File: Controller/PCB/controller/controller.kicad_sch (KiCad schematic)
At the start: 57 parts, among them J1 nRF24L01_Conn, Q1 S9013, Q2 S9013, Q4 S9013, SW1 SW_SPDT, U1 Joystick, U2 Joystick, U3 LM2940-3.0, U5 LM2940-5.0

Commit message: Finalise PCB Design
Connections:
- net Earth: now also U1.EARTH, U2.EARTH
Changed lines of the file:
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@@
     (pin "2")
-  )
-  (symbol (lib_id "power:Earth") (at 68.58 123.19 0) (unit 1)
-    (in_bom yes) (on_board yes)
-    (property "Reference" "#PWR0154" (id 0) (at 68.58 129.54 0)
-      (effects (font (size 1.27 1.27)) hide)
-    )
-    (property "Value" "Earth" (id 1) (at 68.58 127 0)
-      (effects (font (size 1.27 1.27)) hide)
-    )
-    (property "Footprint" "" (id 2) (at 68.58 123.19 0)
-      (effects (font (size 1.27 1.27)) hide)
-    )
-    (property "Datasheet" "~" (id 3) (at 68.58 123.19 0)
-      (effects (font (size 1.27 1.27)) hide)
-    )
-    (pin "1")
   )
   (symbol (lib_id "Device:LED") (at 232.41 22.86 90) (unit 1)
@@
     (pin "1")
     (pin "2")
+  )
+  (symbol (lib_id "power:Earth") (at 68.58 123.19 0) (unit 1)
+    (in_bom yes) (on_board yes)
+    (property "Reference" "#PWR0119" (id 0) (at 68.58 129.54 0)
+      (effects (font (size 1.27 1.27)) hide)
+    )
+    (property "Value" "Earth" (id 1) (at 68.58 127 0)
+      (effects (font (size 1.27 1.27)) hide)
+    )
+    (property "Footprint" "" (id 2) (at 68.58 123.19 0)
+      (effects (font (size 1.27 1.27)) hide)
+    )
+    (property "Datasheet" "~" (id 3) (at 68.58 123.19 0)
+      (effects (font (size 1.27 1.27)) hide)
+    )
+    (pin "1")
   )
   (symbol (lib_id "Device:R") (at 184.15 25.4 180) (unit 1)
@@
     (pin "1")
   )
+  (symbol (lib_id "power:Earth") (at 68.58 165.1 0) (unit 1)
+    (in_bom yes) (on_board yes)
+    (property "Reference" "#PWR0121" (id 0) (at 68.58 171.45 0)
+      (effects (font (size 1.27 1.27)) hide)
+    )
+    (property "Value" "Earth" (id 1) (at 68.58 168.91 0)
+      (effects (font (size 1.27 1.27)) hide)
+    )
+    (property "Footprint" "" (id 2) (at 68.58 165.1 0)
+      (effects (font (size 1.27 1.27)) hide)
+    )
+    (property "Datasheet" "~" (id 3) (at 68.58 165.1 0)
+      (effects (font (size 1.27 1.27)) hide)
+    )
+    (pin "1")
+  )
   (symbol (lib_id "Regulator_Linear:LM1117-5.0") (at 251.46 91.44 0) (unit 1)
     (in_bom yes) (on_board yes)
@@
     (pin "2")
   )
-  (symbol (lib_id "power:Earth") (at 68.58 165.1 0) (unit 1)
-    (in_bom yes) (on_board yes)
-    (property "Reference" "#PWR0155" (id 0) (at 68.58 171.45 0)
-      (effects (font (size 1.27 1.27)) hide)
-    )
-    (property "Value" "Earth" (id 1) (at 68.58 168.91 0)
-      (effects (font (size 1.27 1.27)) hide)
-    )
-    (property "Footprint" "" (id 2) (at 68.58 165.1 0)
-      (effects (font (size 1.27 1.27)) hide)
-    )
-    (property "Datasheet" "~" (id 3) (at 68.58 165.1 0)
-      (effects (font (size 1.27 1.27)) hide)
-    )
-    (pin "1")
-  )
   (symbol (lib_id "power:Earth") (at 151.13 123.19 0) (unit 1)
     (in_bom yes) (on_board yes)
@@
       (reference "#PWR0118") (unit 1) (value "+3.3V") (footprint "")
     )
+    (path "/6454f7b0-7b11-437e-b10a-8dd84dd76148"
+      (reference "#PWR0119") (unit 1) (value "Earth") (footprint "")
+    )
     (path "/00000000-0000-0000-0000-00006213857b"
       (reference "#PWR0120") (unit 1) (value "+3.3V") (footprint "")
     )
+    (path "/76caffeb-621d-4bb0-aa34-92fdde0764be"
+      (reference "#PWR0121") (unit 1) (value "Earth") (footprint "")
+    )
     (path "/00000000-0000-0000-0000-00006208d21d"
       (reference "#PWR0123") (unit 1) (value "+5V") (footprint "")
@@
       (reference "#PWR0153") (unit 1) (value "+BATT") (footprint "")
     )
-    (path "/2c8b76b6-1dc1-42a3-a2cc-221d9612c107"
-      (reference "#PWR0154") (unit 1) (value "Earth") (footprint "")
-    )
-    (path "/cc071879-20c2-476a-8fa9-027c97c88a6e"
-      (reference "#PWR0155") (unit 1) (value "Earth") (footprint "")
-    )
     (path "/8d4725e8-66fd-4c8d-af14-f62e909630d9"

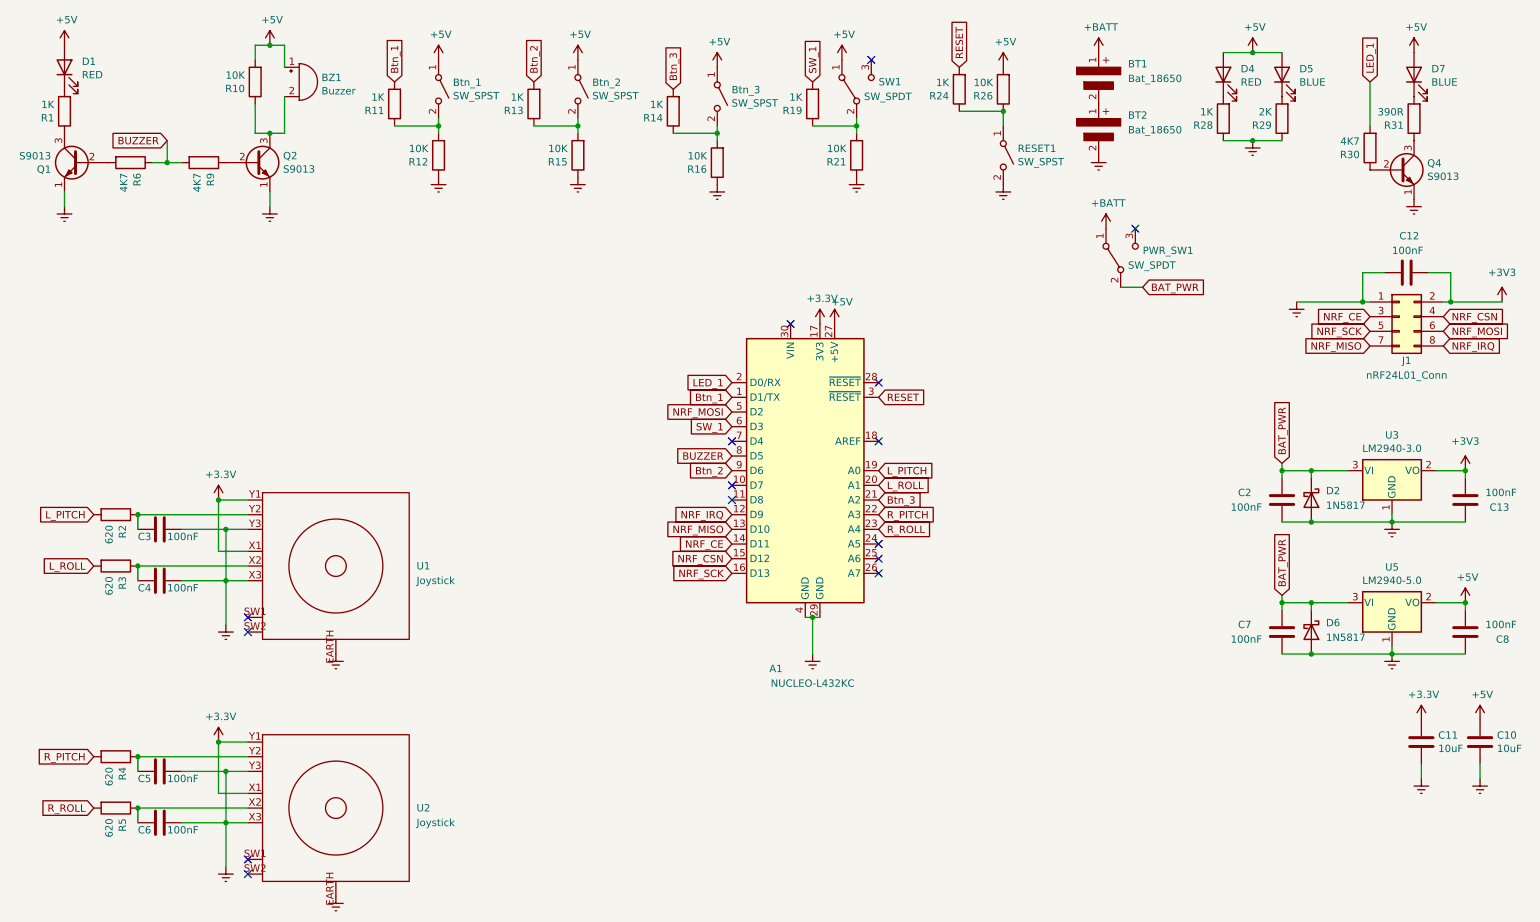
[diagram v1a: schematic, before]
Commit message: Add a voltage level detector circuit
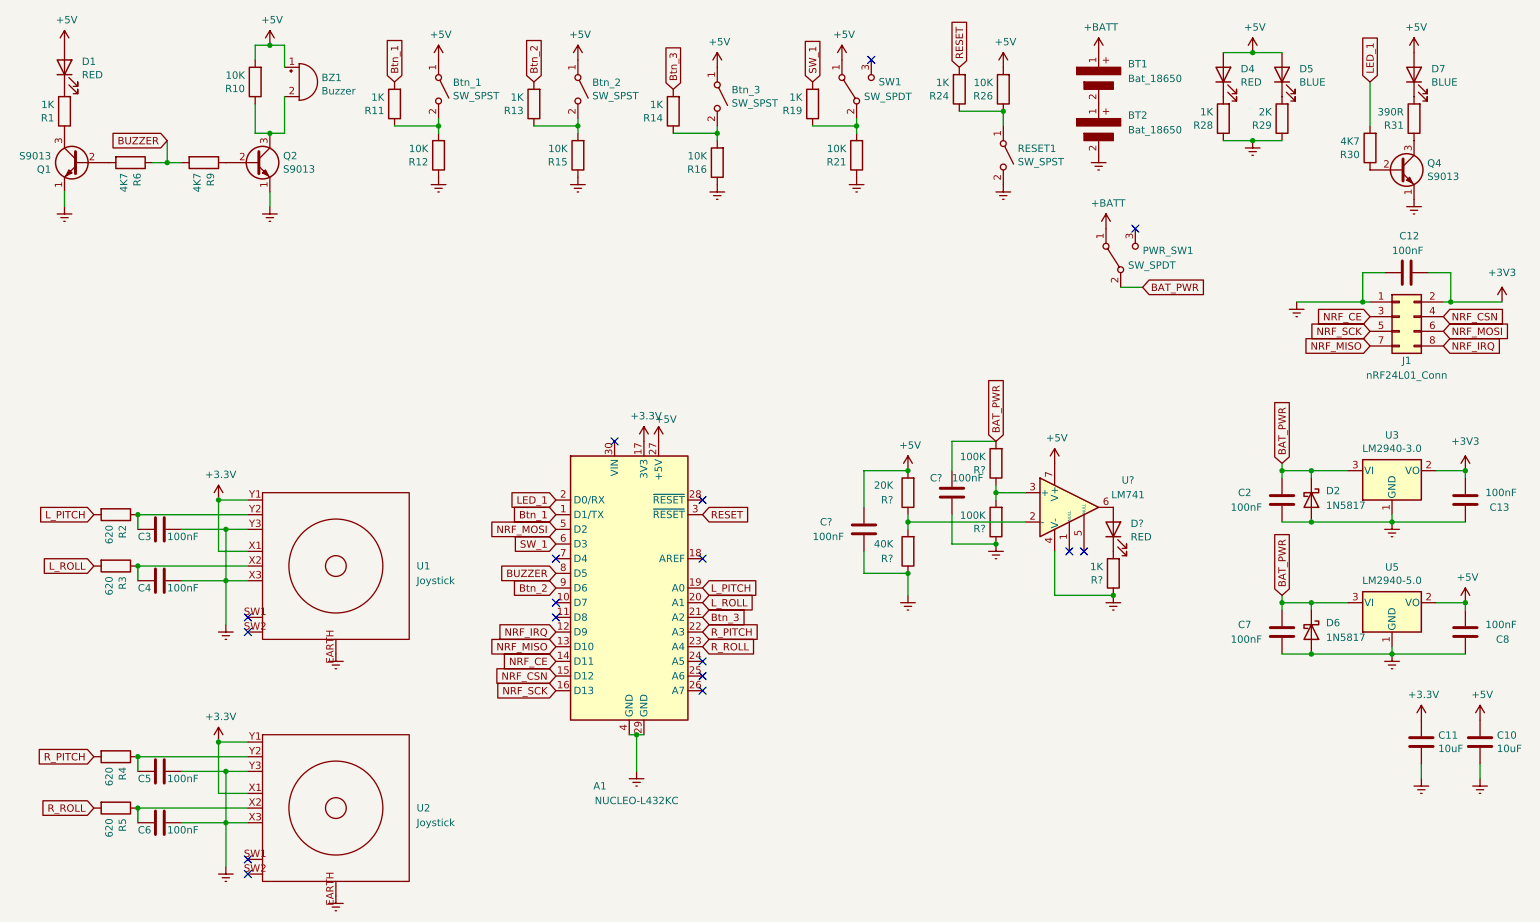
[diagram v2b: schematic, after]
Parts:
- added C? (x2): 100nF, Capacitor_SMD:C_0603_1608Metric, symbol Device:C
- added D?: RED, LED_SMD:LED_0603_1608Metric, symbol Device:LED
- added R?: 20K, Resistor_SMD:R_0603_1608Metric, symbol Device:R
- added R?: 1K, Resistor_SMD:R_0603_1608Metric, symbol Device:R
- added R? (x2): 100K, Resistor_SMD:R_0603_1608Metric, symbol Device:R
- added R?: 40K, Resistor_SMD:R_0603_1608Metric, symbol Device:R
- added U?: LM741, symbol Amplifier_Operational:LM741
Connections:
- net +5V: now also C?.1, R?.2, U?.7 (V+)
- net BAT_PWR: now also C?.1, R?.2
- net Earth: now also C?.2, C?.2, R?.1, R?.1, R?.1, U?.4 (V-)
- new net: R?.1, R?.2, U?.2 (-)
- new net: D?.1 (K), R?.2
- new net: D?.2 (A), U?.6
- new net: R?.1, R?.2, U?.3 (+)
- no-connect marks 15 -> 17
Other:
- moved on the sheet: A1

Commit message: Update controller.kicad_sch
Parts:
- gave numbers to parts that had none: 9

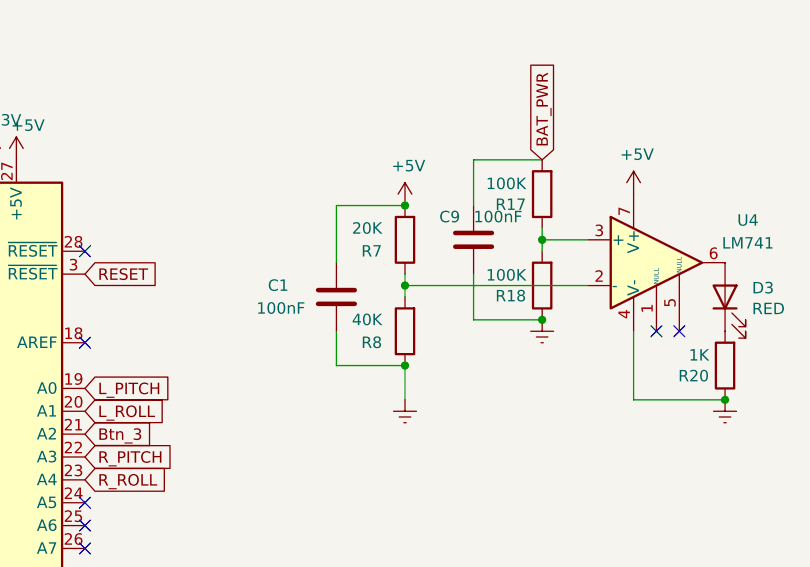
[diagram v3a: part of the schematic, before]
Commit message: Add Trim pot to battery level checker
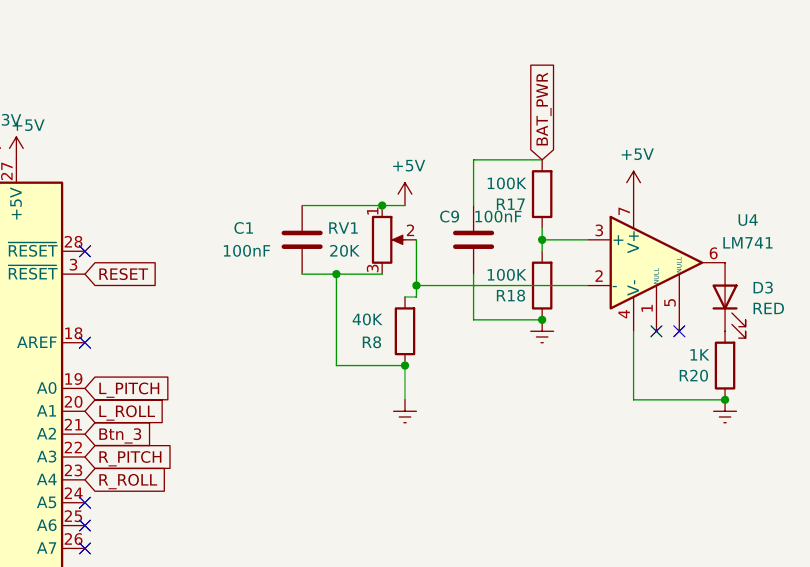
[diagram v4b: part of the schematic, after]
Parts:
- removed R7: 20K, Resistor_SMD:R_0603_1608Metric, symbol Device:R
- added RV1: 20K, My_library:35WR100KLFTR, symbol Device:R_Potentiometer
- U4: footprint (none) -> My_library:741C
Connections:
- net +5V: now also RV1.1
- net Earth: now also RV1.3
- net at R8.2, U4.2 (-): now also RV1.2
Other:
- moved on the sheet: C1

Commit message: Create Gerber files
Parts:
- R1, R11, R13, R14, R19, R20, R24, R28: value 1K -> 2K
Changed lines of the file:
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@@
       (effects (font (size 1.27 1.27)) (justify left))
     )
-    (property "Value" "1K" (id 1) (at 101.092 26.797 0)
+    (property "Value" "2K" (id 1) (at 101.092 26.797 0)
       (effects (font (size 1.27 1.27)) (justify left))
     )
@@
       (effects (font (size 1.27 1.27)) (justify left))
     )
-    (property "Value" "1K" (id 1) (at 174.752 24.257 0)
+    (property "Value" "2K" (id 1) (at 174.752 24.257 0)
       (effects (font (size 1.27 1.27)) (justify left))
     )
@@
       (effects (font (size 1.27 1.27)) (justify left))
     )
-    (property "Value" "1K" (id 1) (at 125.222 28.067 0)
+    (property "Value" "2K" (id 1) (at 125.222 28.067 0)
       (effects (font (size 1.27 1.27)) (justify left))
     )
@@
       (effects (font (size 1.27 1.27)) (justify left))
     )
-    (property "Value" "1K" (id 1) (at 19.812 28.067 0)
+    (property "Value" "2K" (id 1) (at 19.812 28.067 0)
       (effects (font (size 1.27 1.27)) (justify left))
     )
@@
       (effects (font (size 1.27 1.27)) (justify left))
     )
-    (property "Value" "1K" (id 1) (at 201.422 108.077 0)
+    (property "Value" "2K" (id 1) (at 201.422 108.077 0)
       (effects (font (size 1.27 1.27)) (justify left))
     )
@@
       (effects (font (size 1.27 1.27)) (justify left))
     )
-    (property "Value" "1K" (id 1) (at 149.352 26.797 0)
+    (property "Value" "2K" (id 1) (at 149.352 26.797 0)
       (effects (font (size 1.27 1.27)) (justify left))
     )
@@
       (effects (font (size 1.27 1.27)) (justify left))
     )
-    (property "Value" "1K" (id 1) (at 220.472 29.337 0)
+    (property "Value" "2K" (id 1) (at 220.472 29.337 0)
       (effects (font (size 1.27 1.27)) (justify left))
     )
@@
       (effects (font (size 1.27 1.27)) (justify left))
     )
-    (property "Value" "1K" (id 1) (at 76.962 26.797 0)
+    (property "Value" "2K" (id 1) (at 76.962 26.797 0)
       (effects (font (size 1.27 1.27)) (justify left))
     )
@@
     )
     (path "/50cd6d65-818d-4588-8cf3-2b842fdb51d1"
-      (reference "R1") (unit 1) (value "1K") (footprint "Resistor_SMD:R_0603_1608Metric")
+      (reference "R1") (unit 1) (value "2K") (footprint "Resistor_SMD:R_0603_1608Metric")
     )
     (path "/00000000-0000-0000-0000-0000620fbec3"
@@
     )
     (path "/bfbafd4d-bf76-467b-9693-2846d345b89f"
-      (reference "R11") (unit 1) (value "1K") (footprint "Resistor_SMD:R_0603_1608Metric")
+      (reference "R11") (unit 1) (value "2K") (footprint "Resistor_SMD:R_0603_1608Metric")
     )
     (path "/3f70d111-f67a-46d7-995e-20c84abd7e2a"
@@
     )
     (path "/1297c3b9-785a-4268-bb9c-61bc85df5266"
-      (reference "R13") (unit 1) (value "1K") (footprint "Resistor_SMD:R_0603_1608Metric")
+      (reference "R13") (unit 1) (value "2K") (footprint "Resistor_SMD:R_0603_1608Metric")
     )
     (path "/2d3a0ac9-4f99-49dc-b411-811ebd0da77a"
-      (reference "R14") (unit 1) (value "1K") (footprint "Resistor_SMD:R_0603_1608Metric")
+      (reference "R14") (unit 1) (value "2K") (footprint "Resistor_SMD:R_0603_1608Metric")
     )
     (path "/6fdbeb56-e2f8-4f2b-9af2-f7ca1cf76610"
@@
     )
     (path "/6651f224-d4e8-4616-bf2a-577b39fa0a9b"
-      (reference "R19") (unit 1) (value "1K") (footprint "Resistor_SMD:R_0603_1608Metric")
+      (reference "R19") (unit 1) (value "2K") (footprint "Resistor_SMD:R_0603_1608Metric")
     )
     (path "/5f33185c-b454-42a5-b564-5ab8e8d7612f"
-      (reference "R20") (unit 1) (value "1K") (footprint "Resistor_SMD:R_0603_1608Metric")
+      (reference "R20") (unit 1) (value "2K") (footprint "Resistor_SMD:R_0603_1608Metric")
     )
     (path "/3e5bce97-80e4-4698-a6e1-121066cb8cdc"
@@
     )
     (path "/2749ed2b-d13b-4dc8-b662-45e3edf01fc7"
-      (reference "R24") (unit 1) (value "1K") (footprint "Resistor_SMD:R_0603_1608Metric")
+      (reference "R24") (unit 1) (value "2K") (footprint "Resistor_SMD:R_0603_1608Metric")
     )
     (path "/646095b7-764f-4dcf-9d1e-c477304e8894"
@@
     )
     (path "/b2dfb989-192d-4701-bb6f-8735741afa52"
-      (reference "R28") (unit 1) (value "1K") (footprint "Resistor_SMD:R_0603_1608Metric")
+      (reference "R28") (unit 1) (value "2K") (footprint "Resistor_SMD:R_0603_1608Metric")
     )
     (path "/4182e1a5-03a2-4fb0-9267-a43eb1361bf7"

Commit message: Final PCB for controller along with all build and assembly files
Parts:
- removed C10, C11: 10uF, Capacitor_SMD:CP_Elec_4x5.4, symbol Device:C
- removed U4: LM741, My_library:741C, symbol Amplifier_Operational:LM741
- added U4: LM358DR2G, Package_SO:SOP-8_3.76x4.96mm_P1.27mm, symbol Amplifier_Operational:LM358
- D1: value RED -> GREEN
- D2, D6: value 1N5817 -> B5817W-5819W; footprint My_library:1N5817M -> Diode_SMD:D_SOD-123
- D3, D4: value RED -> YELLOW
- R1, R11, R13, R14, R19, R20, R24, R28: value 2K -> 2K2
- R29: value 2K -> 1K
- R31: value 390R -> 1K
- U3: value LM2940-3.0 -> ZSR330GTA
- U5: value LM2940-5.0 -> ZLDO1117G50TA
- renumbered Q4 to Q3
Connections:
- net +5V: now also U4.8 (V+)
- net Earth: now also U4.4 (V-)
- net at R8.2, RV1.2: now also U4.2 (-)
- net at R17.1, R18.2: now also U4.3 (+)
- net at D3.2 (A): now also U4.1
- no-connect marks 17 -> 18

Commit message: Change footprint of RV1 and update gerber files
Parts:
- RV1: footprint My_library:35WR100KLFTR -> My_library:Variable_Resistor
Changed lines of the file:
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@@
       (effects (font (size 1.27 1.27)) (justify right))
     )
-    (property "Footprint" "My_library:35WR100KLFTR" (id 2) (at 165.1 95.25 0)
+    (property "Footprint" "My_library:Variable_Resistor" (id 2) (at 165.1 95.25 0)
       (effects (font (size 1.27 1.27)) hide)
     )
@@
     )
     (path "/5cc4014c-b95b-469d-82a1-798dadb587d3"
-      (reference "RV1") (unit 1) (value "20K") (footprint "My_library:35WR100KLFTR")
+      (reference "RV1") (unit 1) (value "20K") (footprint "My_library:Variable_Resistor")
     )
     (path "/00000000-0000-0000-0000-0000620f8d01"
